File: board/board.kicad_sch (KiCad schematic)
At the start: 21 parts, among them J1 Conn_01x04_Pin, J2 Conn_01x04_Socket, J3 Conn_01x03_Socket, J4 Conn_01x02_Pin, U1 MSP430G2553IN20, U3 NCP1117-3.3_SOT223

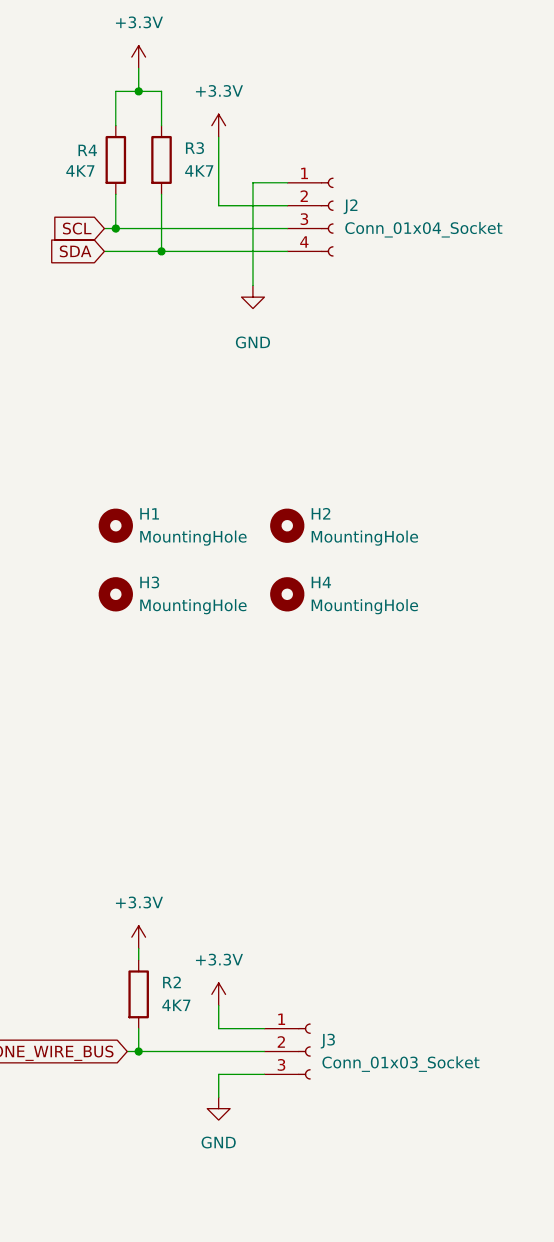
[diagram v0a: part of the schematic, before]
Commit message: Corrected sensor and oled pins
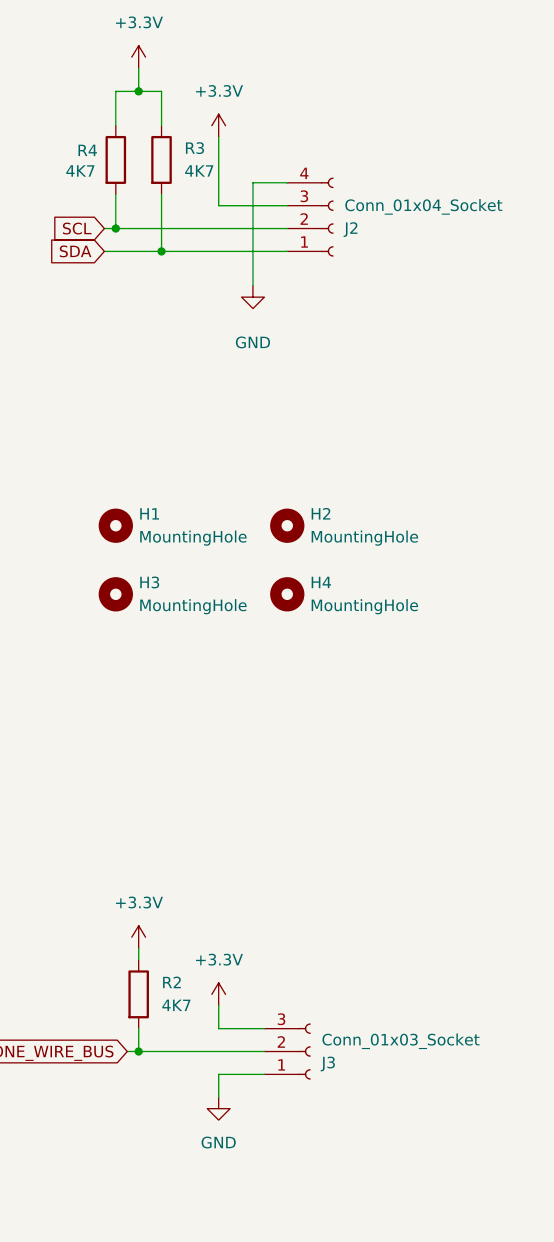
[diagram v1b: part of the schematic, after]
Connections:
- net +3.3V: now also J2.3 (Pin_3), J3.3 (Pin_3); no longer J2.2 (Pin_2), J3.1 (Pin_1)
- net GND: now also J2.4 (Pin_4), J3.1 (Pin_1); no longer J2.1 (Pin_1), J3.3 (Pin_3)
- net SCL: now also J2.2 (Pin_2); no longer J2.3 (Pin_3)
- net SDA: now also J2.1 (Pin_1); no longer J2.4 (Pin_4)
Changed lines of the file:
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@@
 	(symbol
 		(lib_id "Connector:Conn_01x04_Socket")
-		(at 260.35 39.37 0)
-		(unit 1)
-		(exclude_from_sim no)
-		(in_bom yes)
-		(on_board yes)
-		(dnp no)
-		(fields_autoplaced yes)
+		(at 260.35 41.91 0)
+		(mirror x)
+		(unit 1)
+		(exclude_from_sim no)
+		(in_bom yes)
+		(on_board yes)
+		(dnp no)
 		(property "Reference" "J2"
-			(at 261.62 39.3699 0)
+			(at 261.62 41.9101 0)
 			(effects
 				(font
@@
 		)
 		(property "Value" "Conn_01x04_Socket"
-			(at 261.62 41.9099 0)
+			(at 261.62 39.3701 0)
 			(effects
 				(font
@@
 		)
 		(property "Footprint" "Connector_PinSocket_2.54mm:PinSocket_1x04_P2.54mm_Vertical"
-			(at 260.35 39.37 0)
+			(at 260.35 41.91 0)
 			(effects
 				(font
@@
 		)
 		(property "Datasheet" "~"
-			(at 260.35 39.37 0)
+			(at 260.35 41.91 0)
 			(effects
 				(font
@@
 		)
 		(property "Description" "Generic connector, single row, 01x04, script generated"
-			(at 260.35 39.37 0)
+			(at 260.35 41.91 0)
 			(effects
 				(font
@@
 		(lib_id "Connector:Conn_01x03_Socket")
 		(at 257.81 133.35 0)
-		(unit 1)
-		(exclude_from_sim no)
-		(in_bom yes)
-		(on_board yes)
-		(dnp no)
-		(fields_autoplaced yes)
+		(mirror x)
+		(unit 1)
+		(exclude_from_sim no)
+		(in_bom yes)
+		(on_board yes)
+		(dnp no)
 		(property "Reference" "J3"
-			(at 259.08 132.0799 0)
+			(at 259.08 134.6201 0)
 			(effects
 				(font
@@
 		)
 		(property "Value" "Conn_01x03_Socket"
-			(at 259.08 134.6199 0)
-			(effects
-				(font
+			(at 259.08 132.0801 0)
+			(effects
+				(font
